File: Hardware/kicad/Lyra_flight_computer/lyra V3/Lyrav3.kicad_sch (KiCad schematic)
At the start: 80 parts, among them J2 Screw_Terminal_01x06, J3 Conn_01x02, J4 Conn_01x02, J5 Conn_01x03, J6 Conn_01x06, J7 USB_B_Micro, J8 Conn_01x04, J9 Screw_Terminal_01x06, Q1 AO3401A, Q2 AO3400A, Q3 AO3400A, Q4 AO3400A, Q5 AO3400A, U1 AZ1117-3.3, U2 BMI088, U3 BMP388, U4 ADXL375BCCZ-RL7, U6 ADS1015IDGS, U8 RP2040, U9 W25Q128JVS, X1 S3D12.288000B20F30T

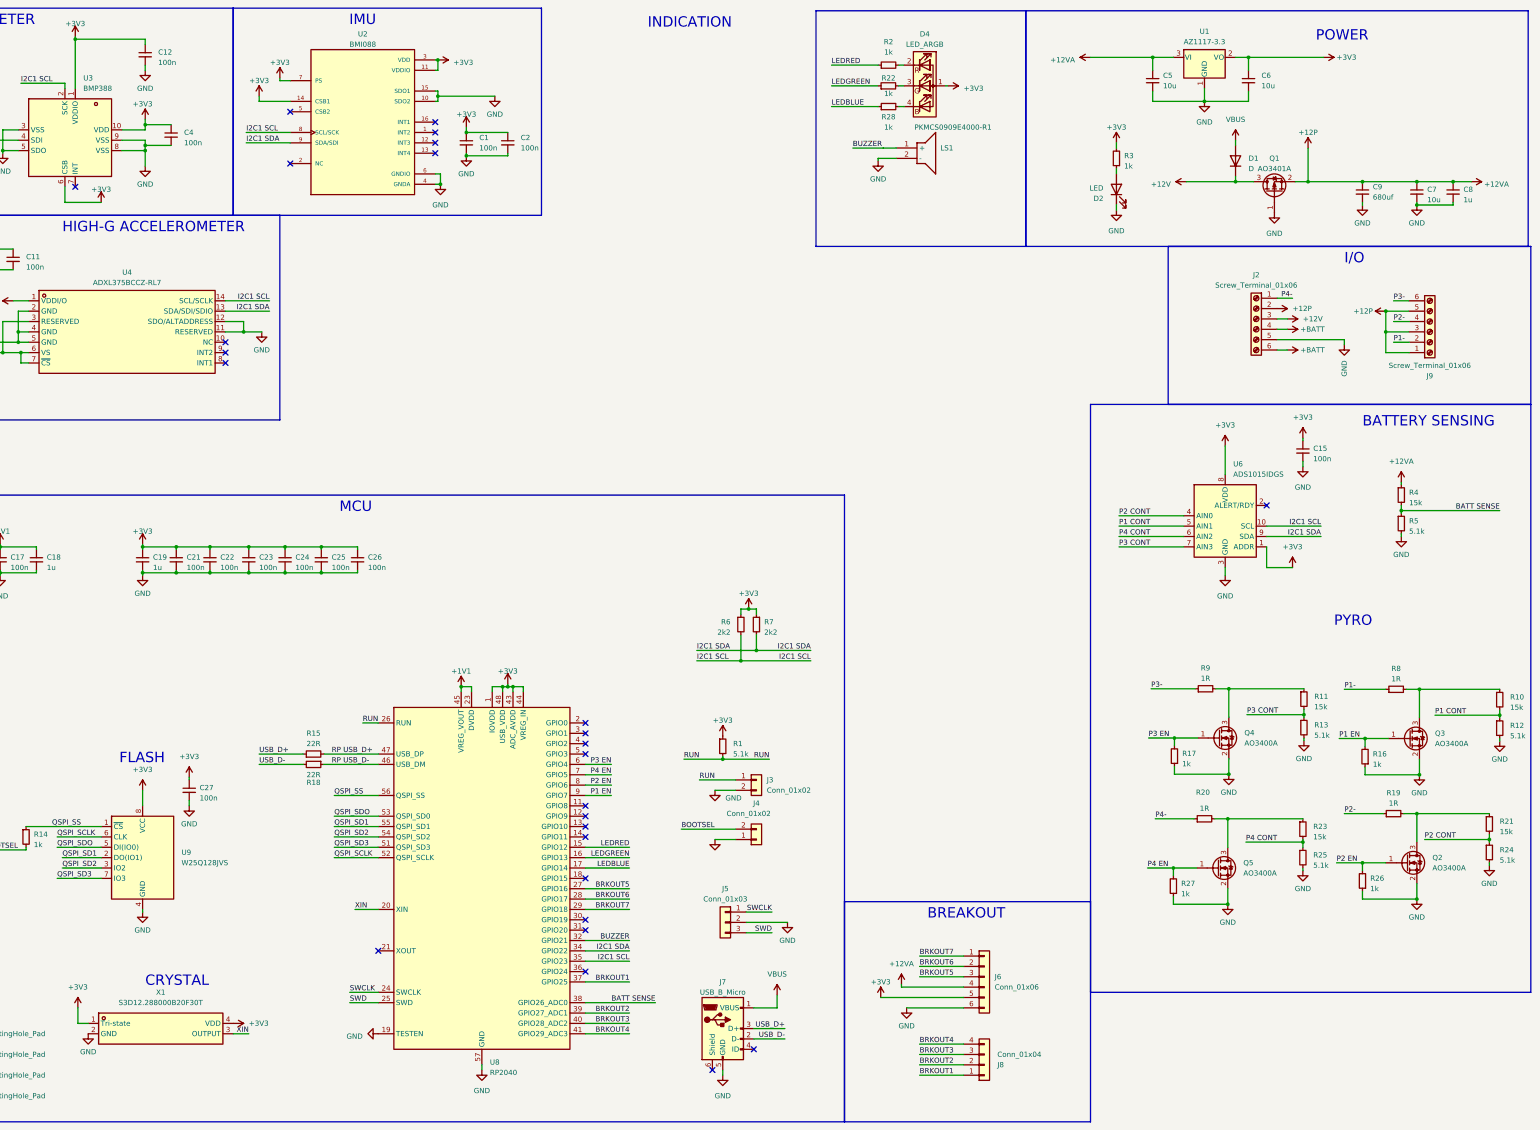
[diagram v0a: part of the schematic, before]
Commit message: add gps module init
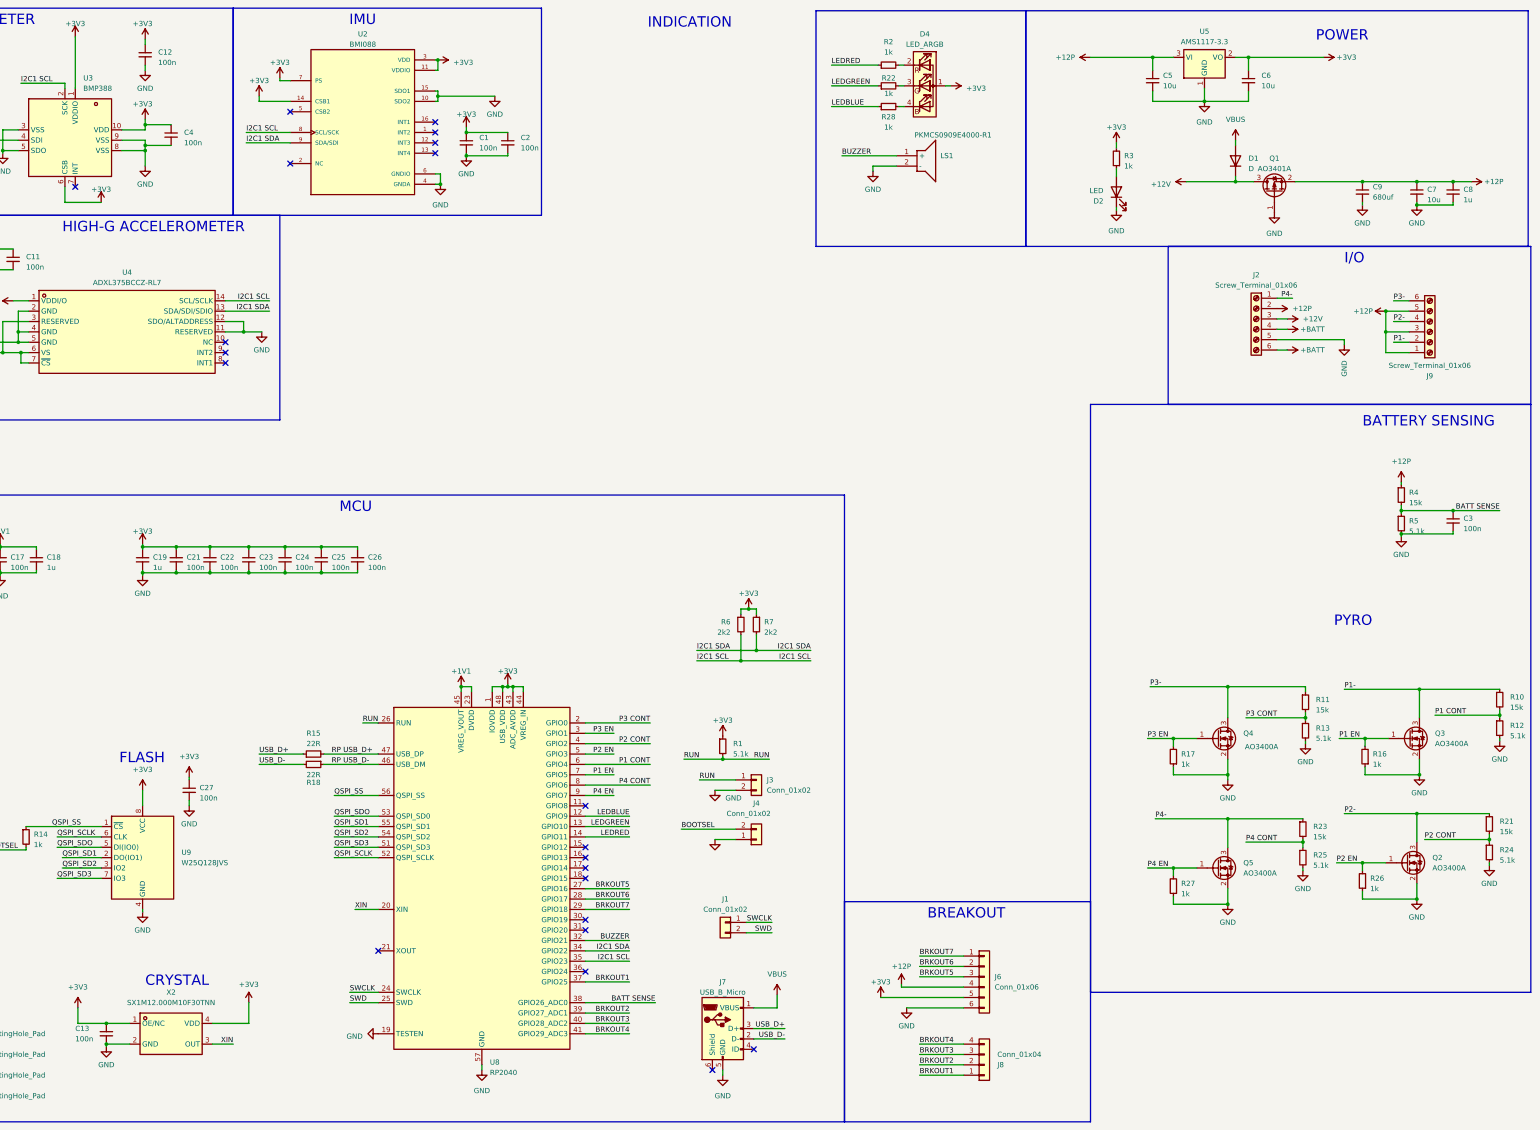
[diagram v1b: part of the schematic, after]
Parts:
- removed C15: 100n, Capacitor_SMD:C_0402_1005Metric, symbol Device:C_Small
- removed J5: Conn_01x03, Connector_PinHeader_2.00mm:PinHeader_1x03_P2.00mm_Vertical, symbol Connector_Generic:Conn_01x03
- removed R19, R20, R8, R9: 1R, Resistor_SMD:R_0603_1608Metric, symbol Device:R_Small
- removed U1: AZ1117-3.3, Package_TO_SOT_SMD:SOT-223, symbol Regulator_Linear:AZ1117-3.3
- removed U6: ADS1015IDGS, easyeda2kicad:X2QFN-10_L2.0-W1.5-P0.50-BL, symbol Analog_ADC:ADS1015IDGS
- removed X1: S3D12.288000B20F30T, easyeda2kicad:OSC-SMD_4P-L3.2-W2.5-BL_SIT8008BI, symbol easyeda2kicad:S3D12.288000B20F30T
- added C13, C3: 100n, Capacitor_SMD:C_0402_1005Metric, symbol Device:C_Small
- added J1: Conn_01x02, Jumper:SolderJumper-2_P1.3mm_Open_Pad1.0x1.5mm, symbol Connector_Generic:Conn_01x02
- added U5: AMS1117-3.3, Package_TO_SOT_SMD:SOT-223-3_TabPin2, symbol Regulator_Linear:AMS1117-3.3
- added X2: SX1M12.000M10F30TNN, easyeda2kicad:OSC-SMD_4P-L2.0-W1.6-BL, symbol easyeda2kicad:SX1M12.000M10F30TNN
- C5, C6, C7: footprint Capacitor_SMD:C_0402_1005Metric -> Capacitor_SMD:C_0603_1608Metric; LCSC Part C15525 -> C96446
- D1: footprint Diode_SMD:D_SOD-323 -> Diode_SMD:D_SOD-123; LCSC Part C2128 -> C64898
- D2: LCSC Part C2297 -> (none)
- R15, R18: LCSC Part C25091 -> C25092
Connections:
- net +12P: now also U5.3 (VI)
- net +3V3: now also C13.1, U5.2 (VO), X2.1 (OE/NC), X2.4 (VDD)
- net BATT SENSE : now also C3.1
- net GND: now also C13.2, C3.2, U5.1 (GND), X2.2 (GND)
- net LEDBLUE: now also U8.12 (GPIO9); no longer U8.17 (GPIO14)
- net LEDGREEN: now also U8.13 (GPIO10); no longer U8.16 (GPIO13)
- net LEDRED: now also U8.14 (GPIO11); no longer U8.15 (GPIO12)
- net P1 CONT : now also U8.6 (GPIO4)
- net P1 EN : now also U8.7 (GPIO5); no longer U8.9 (GPIO7)
- net P1-: now also Q3.3 (D), R10.1
- net P2 CONT : now also U8.4 (GPIO2)
- net P2 EN : now also U8.5 (GPIO3); no longer U8.8 (GPIO6)
- net P2-: now also Q2.3 (D), R21.1
- net P3 CONT : now also U8.2 (GPIO0)
- net P3 EN : now also U8.3 (GPIO1); no longer U8.6 (GPIO4)
- net P3-: now also Q4.3 (D), R11.1
- net P4 CONT : now also U8.8 (GPIO6)
- net P4 EN : now also U8.9 (GPIO7); no longer U8.7 (GPIO5)
- net P4-: now also Q5.3 (D), R23.1
- net SWCLK: now also J1.1 (Pin_1)
- net SWD: now also J1.2 (Pin_2)
- net XIN: now also X2.3 (OUT)
- no-connect marks 26 -> 21
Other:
- moved on the sheet: D2, LS1, R11, R13

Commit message: asd
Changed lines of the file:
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@@
   (junction (at 366.395 221.615) (diameter 0) (color 0 0 0 0)
   )
-  (junction (at 375.92 140.97) (diameter 0) (color 0 0 0 0)
-  )
   (junction (at 352.425 186.055) (diameter 0) (color 0 0 0 0)
   )
@@
   (junction (at 67.945 45.72) (diameter 0) (color 0 0 0 0)
   )
+  (junction (at 375.92 141.605) (diameter 0) (color 0 0 0 0)
+  )
   (junction (at 32.385 144.145) (diameter 0) (color 0 0 0 0)
   )
@@
     (stroke (width 0) (type default))
   )
-  (wire (pts (xy 388.62 140.335) (xy 388.62 140.97))
+  (wire (pts (xy 388.62 140.335) (xy 388.62 141.605))
     (stroke (width 0) (type default))
   )
@@
     (stroke (width 0) (type default))
   )
-  (wire (pts (xy 375.92 140.97) (xy 388.62 140.97))
+  (wire (pts (xy 375.92 141.605) (xy 388.62 141.605))
     (stroke (width 0) (type default))
   )
@@
     (stroke (width 0) (type default))
   )
+  (wire (pts (xy 375.92 142.24) (xy 375.92 141.605))
+    (stroke (width 0) (type default))
+  )
   (wire (pts (xy 67.31 144.145) (xy 75.565 144.145))
     (stroke (width 0) (type default))
@@
     )
   )
-  (symbol (lib_id "power:GND") (at 375.92 141.605 0) (unit 1)
+  (symbol (lib_id "power:GND") (at 375.92 142.24 0) (unit 1)
     (in_bom yes) (on_board yes) (dnp no) (fields_autoplaced)
-    (property "Reference" "#PWR050" (at 375.92 147.955 0)
+    (property "Reference" "#PWR050" (at 375.92 148.59 0)
       (effects (font (size 1.27 1.27)) hide)
     )
-    (property "Value" "GND" (at 375.92 146.05 0)
+    (property "Value" "GND" (at 375.92 146.685 0)
       (effects (font (size 1.27 1.27)))
     )
-    (property "Footprint" "" (at 375.92 141.605 0)
+    (property "Footprint" "" (at 375.92 142.24 0)
       (effects (font (size 1.27 1.27)) hide)
     )
-    (property "Datasheet" "" (at 375.92 141.605 0)
+    (property "Datasheet" "" (at 375.92 142.24 0)
       (effects (font (size 1.27 1.27)) hide)
     )
@@
   )
   (symbol (lib_id "power:GND") (at 327.66 34.925 0) (unit 1)
-    (in_bom yes) (on_board yes) (dnp no) (fields_autoplaced)
+    (in_bom yes) (on_board yes) (dnp no)
     (property "Reference" "#PWR08" (at 327.66 41.275 0)
       (effects (font (size 1.27 1.27)) hide)
